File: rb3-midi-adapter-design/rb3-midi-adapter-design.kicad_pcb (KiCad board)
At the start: 2 copper layers, 91.4 x 22.9 mm, 23 parts, among them J1 DIN-5_180degree, J2 USB_B, SW1 SW_Push, U1 ATmega32U4-MU, U2 6N138, Y1 16MHz

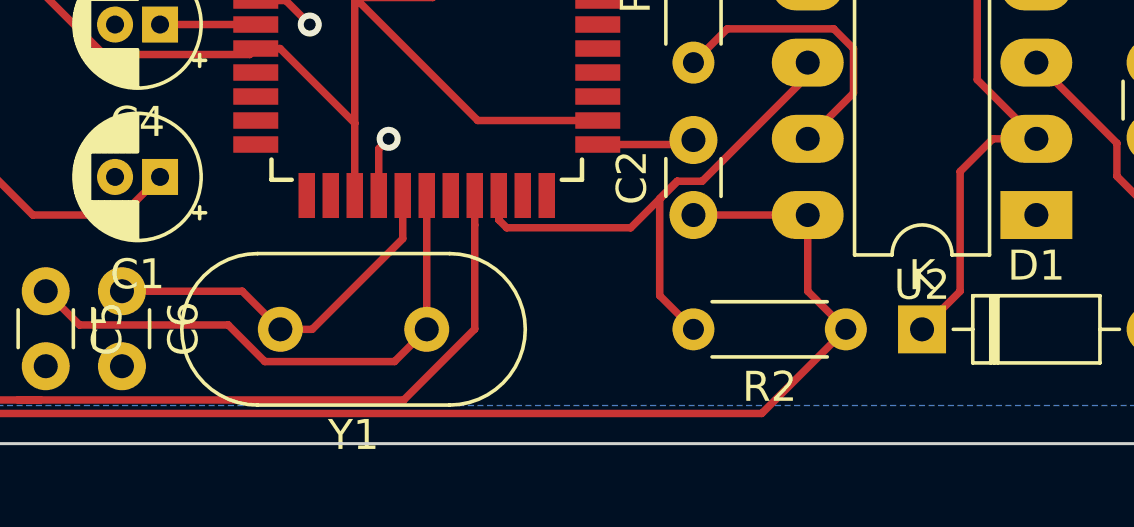
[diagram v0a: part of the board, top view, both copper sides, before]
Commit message: Update KiCad project files to latest version
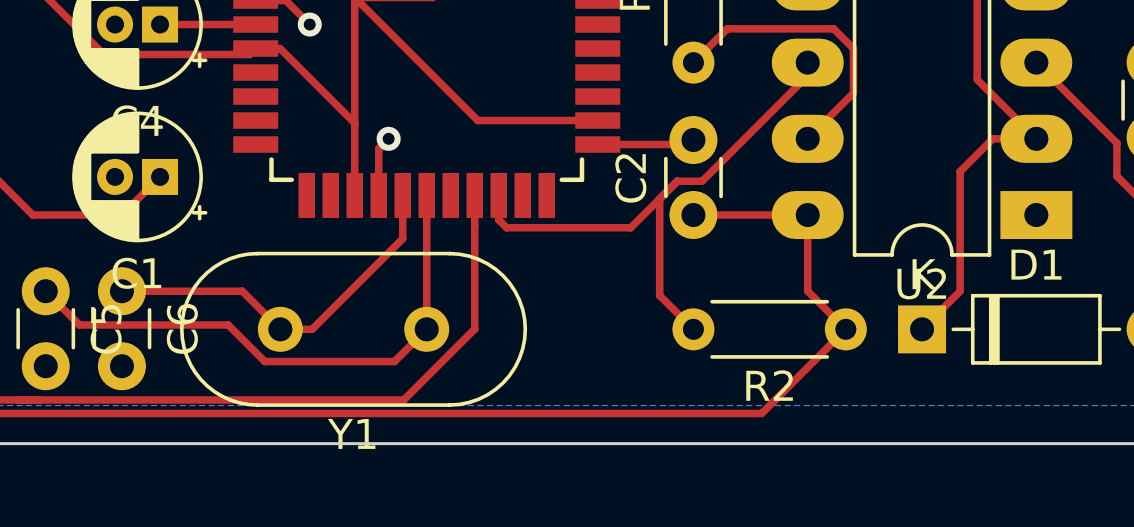
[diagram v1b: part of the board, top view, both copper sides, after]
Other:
- net class Default removed
